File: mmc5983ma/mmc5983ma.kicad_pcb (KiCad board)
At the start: 2 copper layers, 14.5 x 20.5 mm, 7 parts, among them J1 Conn_01x07, U1 MMC5983MA

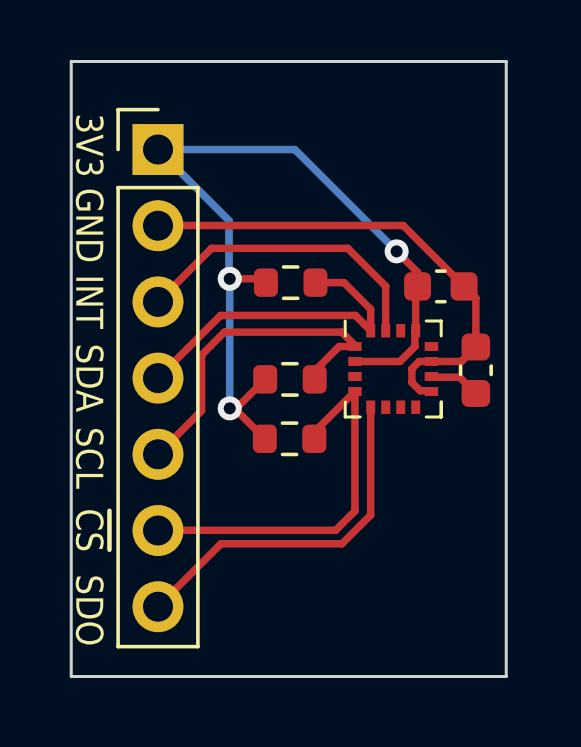
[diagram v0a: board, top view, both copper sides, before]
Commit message: Slight modification to mmc and add ICP-20100
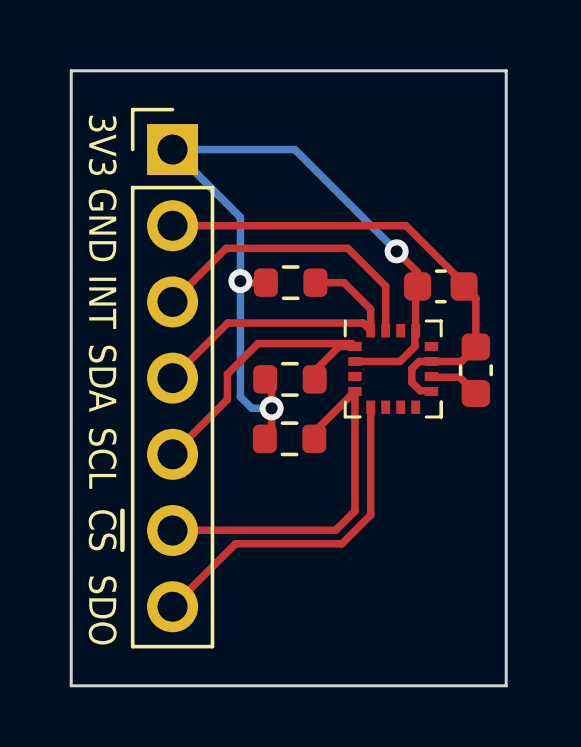
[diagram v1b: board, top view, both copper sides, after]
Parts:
- moved J1 0.49 mm to (103.4, 102.6)
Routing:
- net /SCL: track 11.5 -> 10.1 mm
- net +3V3: track 29.1 -> 28.0 mm
- net /SDA: track 11.1 -> 10.4 mm

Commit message: Slight modifications to boards and add export files
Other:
- board text added: "Designed By: Kush Nayak AmadorUAVs"
- board text added: "MMC5983MA Breakout Board"
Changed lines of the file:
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@@
       (outputformat 1)
       (mirror false)
-      (drillshape 1)
+      (drillshape 0)
       (scaleselection 1)
-      (outputdirectory "")
+      (outputdirectory "export/")
     )
   )
@@
   )
   (gr_rect (start 100 100) (end 114.5 120.5) (layer "Edge.Cuts") (width 0.1) (fill none))
+  (gr_text "Designed By: Kush Nayak\nAmadorUAVs" (at 112.268 111.506 90) (layer "B.SilkS")
+    (effects (font (size 0.8 0.8) (thickness 0.15)) (justify mirror))
+  )
   (gr_text "SDA" (at 101.0158 110.236 270) (layer "F.SilkS")
     (effects (font (size 0.9 0.8) (thickness 0.15)))
@@
     (effects (font (size 0.9 0.8) (thickness 0.15)))
   )
+  (gr_text "MMC5983MA \nBreakout Board" (at 109.474 117.856) (layer "F.SilkS")
+    (effects (font (size 0.8 0.8) (thickness 0.15)))
+  )
   (gr_text "GND" (at 101.0158 105.156 270) (layer "F.SilkS")
